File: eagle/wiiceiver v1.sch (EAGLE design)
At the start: 15 parts, among them IC1 ATmega328P, IC2 317T

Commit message: ordered!
“final” version, ordered from OshPark
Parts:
- added C3: 0.1pF, capacitor-wima:C5/2.5
- CLK: device pinhead:PINHD-1X3 -> crystal:IXFA
- IC1: device ic-package:DIL28 -> ic-package:DIL28-3
- IC2: value 317T -> (none); device linear:317T -> v-reg:LM317TS
- R5, R6, R7, R8: device rcl:R-US_0207/7 -> resistor:R-US_0204/2V
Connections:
- removed net N$12: IC1.1, R8.1, SV1.5
- new net N$2: IC1.1, R8.2, SV1.5
- net GND: now also C3.2
- net N$10: now also IC2.IN; no longer IC2.VI
- net N$16: now also IC2.OUT; no longer IC2.VO
- net VIN: now also C3.1, R8.1; no longer R8.2
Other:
- moved on the sheet: R8

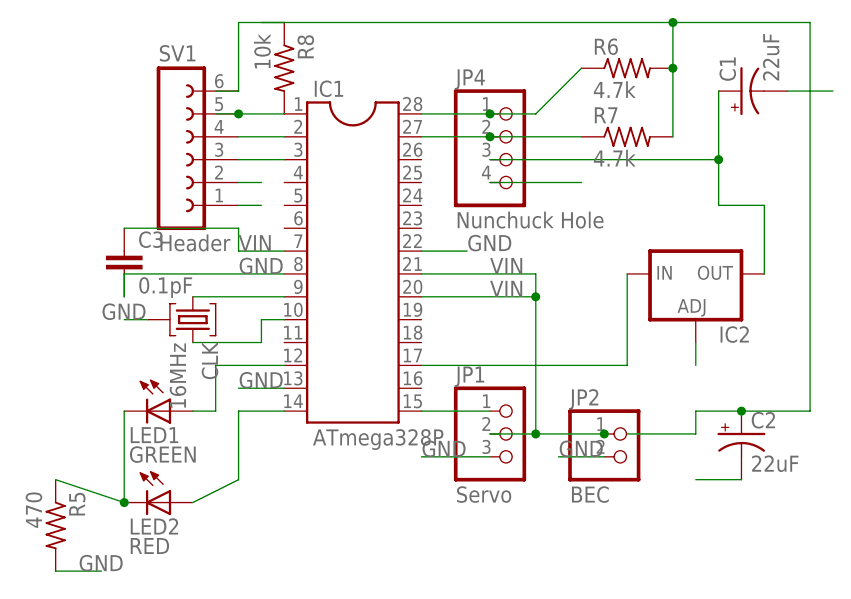
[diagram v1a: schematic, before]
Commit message: updating PCB slightly
6-pin header was a little tight…
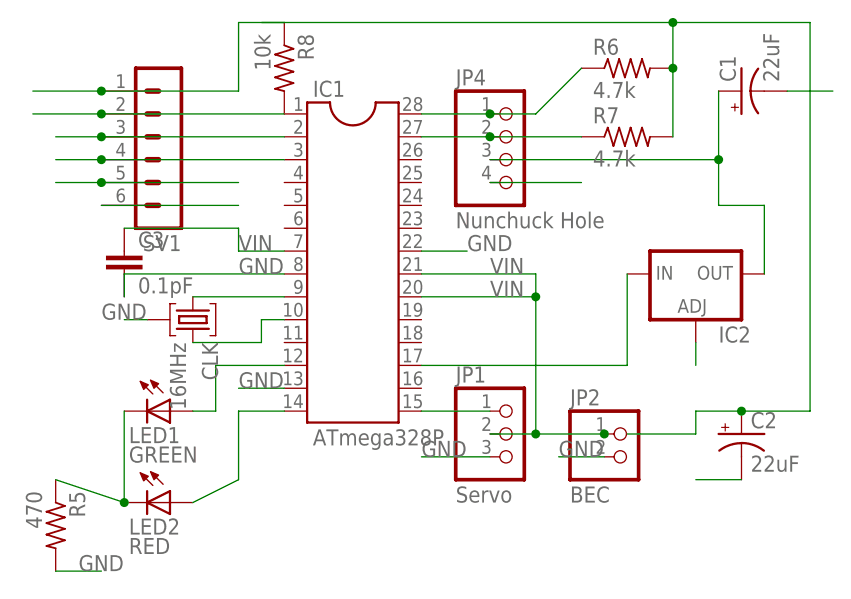
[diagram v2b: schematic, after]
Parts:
- SV1: value Header -> (none); device con-lsta:FE06-1 -> con-lstb:MA06-1
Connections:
- net GND: now also SV1.5, SV1.6; no longer SV1.1, SV1.2
- net N$2: now also SV1.2; no longer SV1.5
- net RX: now also SV1.3; no longer SV1.4
- net TX: now also SV1.4; no longer SV1.3
- net VIN: now also SV1.1; no longer SV1.6
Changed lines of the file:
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@@
 <part name="LED1" library="led" deviceset="LED" device="3MM" value="GREEN"/>
 <part name="LED2" library="led" deviceset="LED" device="3MM" value="RED"/>
-<part name="SV1" library="con-lsta" deviceset="FE06-1" device="" value="Header"/>
 <part name="JP1" library="pinhead" deviceset="PINHD-1X3" device="" value="Servo"/>
 <part name="JP2" library="pinhead" deviceset="PINHD-1X2" device="" value="BEC"/>
@@
 <part name="C3" library="capacitor-wima" deviceset="C" device="5/2.5" value="0.1pF"/>
 <part name="IC2" library="v-reg" deviceset="LM317TS" device=""/>
+<part name="SV1" library="con-lstb" deviceset="MA06-1" device=""/>
 </parts>
 <sheets>
@@
 <instance part="LED1" gate="G$1" x="53.34" y="76.2" rot="R270"/>
 <instance part="LED2" gate="G$1" x="53.34" y="66.04" rot="R270"/>
-<instance part="SV1" gate="G$1" x="53.34" y="104.14"/>
 <instance part="JP1" gate="A" x="91.44" y="73.66"/>
 <instance part="JP2" gate="G$1" x="104.14" y="71.12"/>
@@
 <instance part="C3" gate="G$1" x="48.26" y="93.98"/>
 <instance part="IC2" gate="1" x="111.76" y="91.44"/>
+<instance part="SV1" gate="1" x="53.34" y="104.14" rot="R180"/>
 </instances>
 <busses>
@@
 <net name="RX" class="0">
 <segment>
-<pinref part="SV1" gate="G$1" pin="4"/>
 <pinref part="IC1" gate="G$1" pin="2"/>
-<wire x1="60.96" y1="106.68" x2="66.04" y2="106.68" width="0.1524" layer="91"/>
+<wire x1="66.04" y1="106.68" x2="45.72" y2="106.68" width="0.1524" layer="91"/>
+<pinref part="SV1" gate="1" pin="3"/>
+<wire x1="45.72" y1="106.68" x2="40.64" y2="106.68" width="0.1524" layer="91"/>
+<junction x="45.72" y="106.68"/>
 </segment>
 </net>
@@
 </segment>
 <segment>
-<pinref part="SV1" gate="G$1" pin="1"/>
-<wire x1="60.96" y1="99.06" x2="63.5" y2="99.06" width="0.1524" layer="91"/>
-</segment>
-<segment>
-<pinref part="SV1" gate="G$1" pin="2"/>
-<wire x1="60.96" y1="101.6" x2="63.5" y2="101.6" width="0.1524" layer="91"/>
+<pinref part="SV1" gate="1" pin="6"/>
+<wire x1="45.72" y1="99.06" x2="60.96" y2="99.06" width="0.1524" layer="91"/>
+</segment>
+<segment>
+<wire x1="60.96" y1="101.6" x2="45.72" y2="101.6" width="0.1524" layer="91"/>
+<pinref part="SV1" gate="1" pin="5"/>
+<wire x1="45.72" y1="101.6" x2="40.64" y2="101.6" width="0.1524" layer="91"/>
+<junction x="45.72" y="101.6"/>
 </segment>
 <segment>
@@
 <pinref part="C2" gate="G$1" pin="+"/>
 <wire x1="111.76" y1="76.2" x2="116.84" y2="76.2" width="0.1524" layer="91"/>
-<pinref part="SV1" gate="G$1" pin="6"/>
 <wire x1="66.04" y1="119.38" x2="109.22" y2="119.38" width="0.1524" layer="91"/>
 <wire x1="109.22" y1="119.38" x2="124.46" y2="119.38" width="0.1524" layer="91"/>
@@
 <junction x="109.22" y="119.38"/>
 <junction x="116.84" y="76.2"/>
-<wire x1="58.42" y1="111.76" x2="60.96" y2="111.76" width="0.1524" layer="91"/>
+<wire x1="38.1" y1="111.76" x2="45.72" y2="111.76" width="0.1524" layer="91"/>
+<wire x1="45.72" y1="111.76" x2="60.96" y2="111.76" width="0.1524" layer="91"/>
 <wire x1="60.96" y1="111.76" x2="60.96" y2="119.38" width="0.1524" layer="91"/>
 <pinref part="R8" gate="G$1" pin="1"/>
 <wire x1="63.5" y1="119.38" x2="66.04" y2="119.38" width="0.1524" layer="91"/>
 <wire x1="60.96" y1="119.38" x2="66.04" y2="119.38" width="0.1524" layer="91"/>
+<pinref part="SV1" gate="1" pin="1"/>
+<junction x="45.72" y="111.76"/>
 </segment>
 </net>
@@
 <segment>
 <pinref part="IC1" gate="G$1" pin="3"/>
-<pinref part="SV1" gate="G$1" pin="3"/>
-<wire x1="66.04" y1="104.14" x2="60.96" y2="104.14" width="0.1524" layer="91"/>
+<wire x1="66.04" y1="104.14" x2="45.72" y2="104.14" width="0.1524" layer="91"/>
+<pinref part="SV1" gate="1" pin="4"/>
+<wire x1="45.72" y1="104.14" x2="40.64" y2="104.14" width="0.1524" layer="91"/>
+<junction x="45.72" y="104.14"/>
 </segment>
 </net>
 <net name="N$2" class="0">
 <segment>
-<pinref part="SV1" gate="G$1" pin="5"/>
-<junction x="60.96" y="109.22"/>
 <pinref part="IC1" gate="G$1" pin="1"/>
-<wire x1="60.96" y1="109.22" x2="58.42" y2="109.22" width="0.1524" layer="91"/>
+<wire x1="66.04" y1="109.22" x2="45.72" y2="109.22" width="0.1524" layer="91"/>
 <pinref part="R8" gate="G$1" pin="2"/>
-<wire x1="66.04" y1="109.22" x2="60.96" y2="109.22" width="0.1524" layer="91"/>
-</segment>
-</net>
+<pinref part="SV1" gate="1" pin="2"/>
+<wire x1="45.72" y1="109.22" x2="38.1" y2="109.22" width="0.1524" layer="91"/>
+<junction x="45.72" y="109.22"/>
+</segment>
+</net>
